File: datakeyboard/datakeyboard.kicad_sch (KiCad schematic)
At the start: 48 parts, among them Q1 BSS83P, Q2 BSS83P, Q3 BSS83P, Q4 BSS83P, Q5 BSS83P, SW1 SW_Push, SW2 SW_Push, SW3 SW_Push, SW4 SW_Push, SW5 SW_Push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

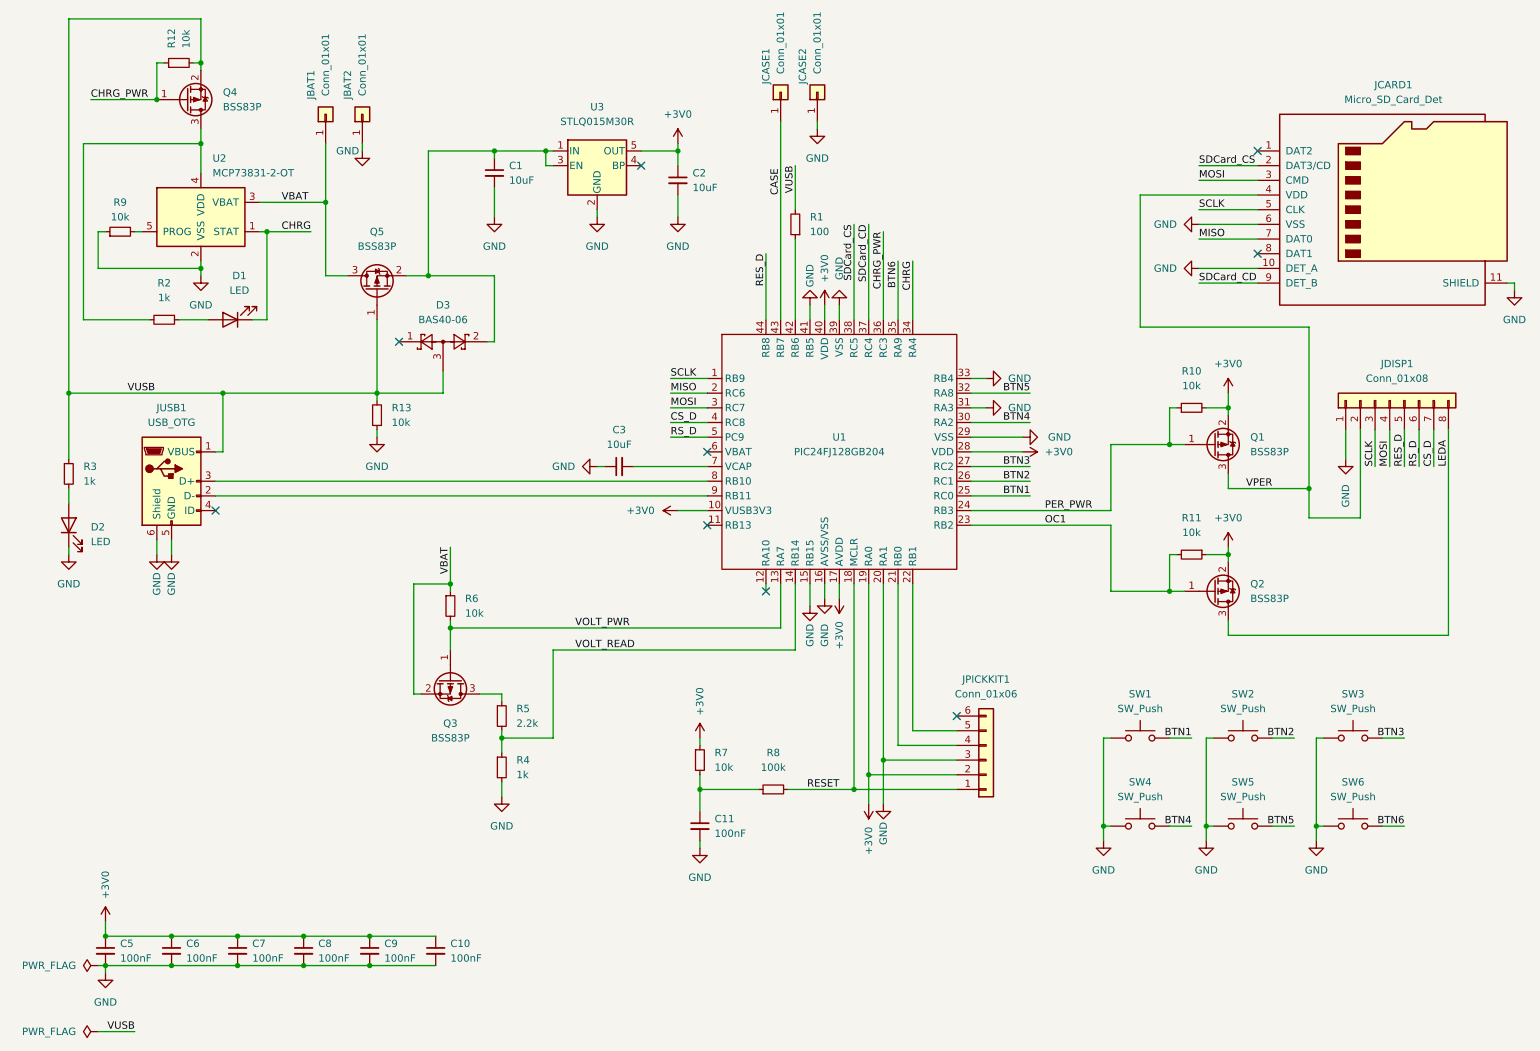
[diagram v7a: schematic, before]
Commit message: Added 3D Model for housing
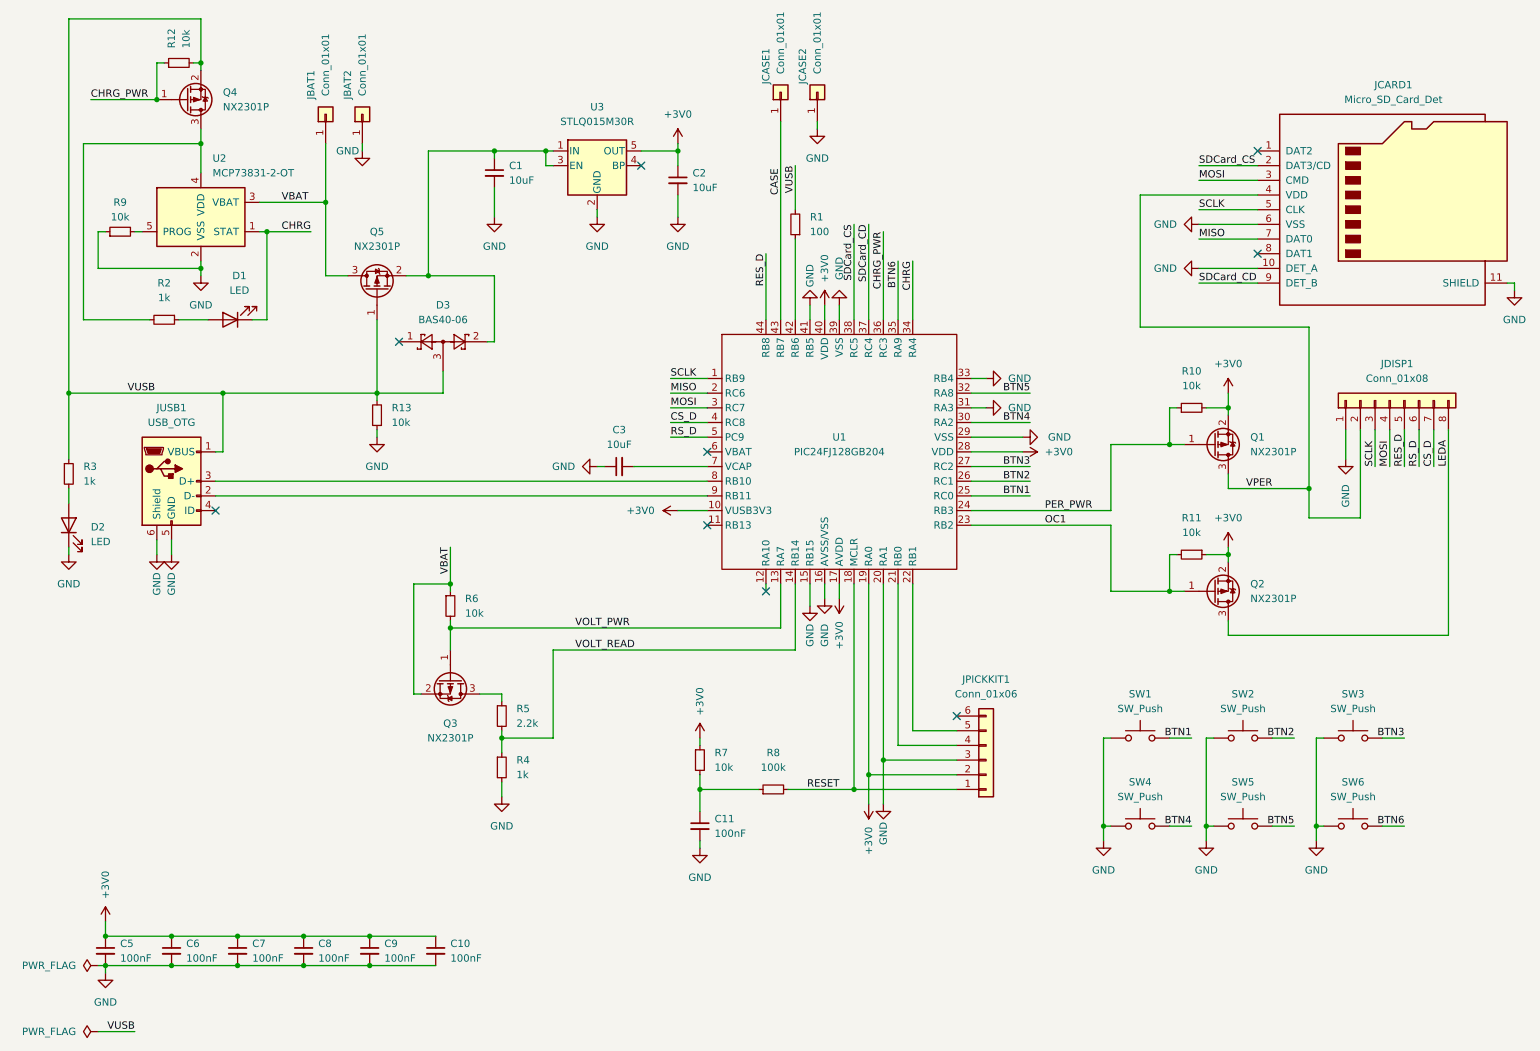
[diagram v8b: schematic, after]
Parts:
- Q1, Q2, Q3, Q4, Q5: value BSS83P -> NX2301P
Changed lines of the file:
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@@
       (effects (font (size 1.27 1.27)) (justify left))
     )
-    (property "Value" "BSS83P" (id 1) (at 226.06 90.1699 0)
+    (property "Value" "NX2301P" (id 1) (at 226.06 90.1699 0)
       (effects (font (size 1.27 1.27)) (justify left))
     )
@@
       (effects (font (size 1.27 1.27)) (justify left))
     )
-    (property "Value" "BSS83P" (id 1) (at 48.26 30.4799 0)
+    (property "Value" "NX2301P" (id 1) (at 48.26 30.4799 0)
       (effects (font (size 1.27 1.27)) (justify left))
     )
@@
     (in_bom yes) (on_board yes) (fields_autoplaced)
     (property "Reference" "Q5" (id 0) (at 74.93 52.07 90))
-    (property "Value" "BSS83P" (id 1) (at 74.93 54.61 90))
+    (property "Value" "NX2301P" (id 1) (at 74.93 54.61 90))
     (property "Footprint" "Package_TO_SOT_SMD:SOT-23" (id 2) (at 76.835 57.15 0)
       (effects (font (size 1.27 1.27) italic) (justify left) hide)
@@
       (effects (font (size 1.27 1.27)) (justify left))
     )
-    (property "Value" "BSS83P" (id 1) (at 226.06 115.5699 0)
+    (property "Value" "NX2301P" (id 1) (at 226.06 115.5699 0)
       (effects (font (size 1.27 1.27)) (justify left))
     )
@@
     (in_bom yes) (on_board yes) (fields_autoplaced)
     (property "Reference" "Q3" (id 0) (at 87.63 137.16 90))
-    (property "Value" "BSS83P" (id 1) (at 87.63 139.7 90))
+    (property "Value" "NX2301P" (id 1) (at 87.63 139.7 90))
     (property "Footprint" "Package_TO_SOT_SMD:SOT-23" (id 2) (at 85.725 134.62 0)
       (effects (font (size 1.27 1.27) italic) (justify left) hide)
@@
     )
     (path "/14f0f55b-770f-492a-a96d-c71bf97952d8"
-      (reference "Q1") (unit 1) (value "BSS83P") (footprint "Package_TO_SOT_SMD:SOT-23")
+      (reference "Q1") (unit 1) (value "NX2301P") (footprint "Package_TO_SOT_SMD:SOT-23")
     )
     (path "/a2ec67e7-2261-45d1-ac8f-b2e4eab51968"
-      (reference "Q2") (unit 1) (value "BSS83P") (footprint "Package_TO_SOT_SMD:SOT-23")
+      (reference "Q2") (unit 1) (value "NX2301P") (footprint "Package_TO_SOT_SMD:SOT-23")
     )
     (path "/d9c84ee2-163c-41c5-ade4-527ccc758a96"
-      (reference "Q3") (unit 1) (value "BSS83P") (footprint "Package_TO_SOT_SMD:SOT-23")
+      (reference "Q3") (unit 1) (value "NX2301P") (footprint "Package_TO_SOT_SMD:SOT-23")
     )
     (path "/37ca8a1c-f48c-4060-9620-ab4075a84731"
-      (reference "Q4") (unit 1) (value "BSS83P") (footprint "Package_TO_SOT_SMD:SOT-23")
+      (reference "Q4") (unit 1) (value "NX2301P") (footprint "Package_TO_SOT_SMD:SOT-23")
     )
     (path "/93f18e25-dbc8-46c4-9e73-08981bfb6cbb"
-      (reference "Q5") (unit 1) (value "BSS83P") (footprint "Package_TO_SOT_SMD:SOT-23")
+      (reference "Q5") (unit 1) (value "NX2301P") (footprint "Package_TO_SOT_SMD:SOT-23")
     )
     (path "/f5dfac85-0fba-4fec-986d-820052834f83"
